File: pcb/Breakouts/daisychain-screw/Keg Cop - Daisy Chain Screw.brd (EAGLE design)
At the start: 33.2 x 43.2 mm, 3 parts, among them J1 0533240360

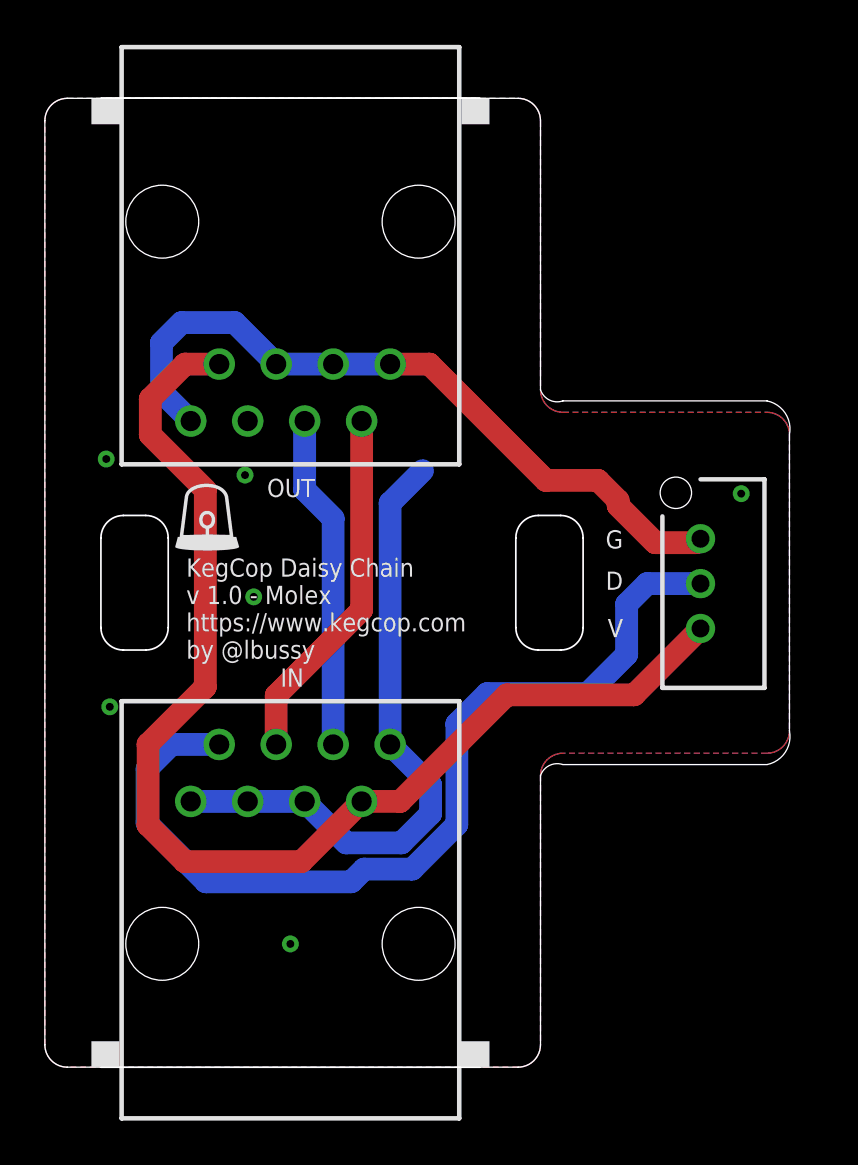
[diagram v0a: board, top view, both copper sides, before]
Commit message: Reorganize daisy chain boards
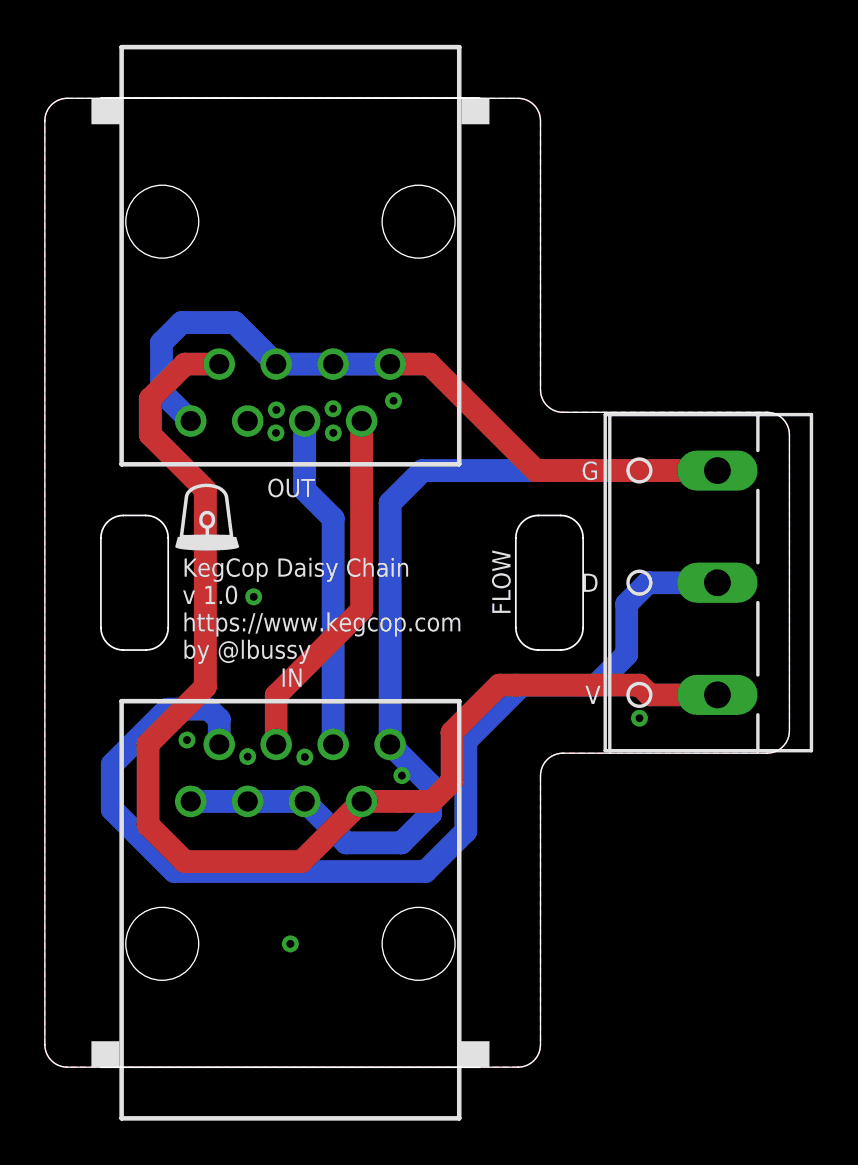
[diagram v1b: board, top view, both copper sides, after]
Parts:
- removed J1: 0533240360, SamacSys_Parts:0533240360
- added FLOW: (no value), con-wago-500:W237-103
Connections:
- net 5VD: now also FLOW.1; no longer J1.3
- net DATA0: now also FLOW.2; no longer J1.2
- net GND: now also FLOW.3; no longer J1.1
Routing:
- net GND: track 61.4 -> 73.7 mm, vias 6 -> 12
- net DATA0: track 41.3 -> 46.2 mm
- net 5VD: track 54.4 -> 55.6 mm
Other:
- outline, holes or cut-outs redrawn
- board text added: "KegCop Daisy Chain v 1.0 https://www.kegcop.com by @lbussy"
- board text removed: "KegCop Daisy Chain v 1.0 - Molex https://www.kegcop.com by @lbussy"
